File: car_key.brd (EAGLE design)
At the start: 160 x 100 mm, 2 parts, among them U2 ATMEGA328P-AU

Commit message: Major additions
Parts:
- added C10: 1pF, resistor:C0805
- added C11: 2.2nF, resistor:C0805
- added C12: 4.7pF, resistor:C0805
- added C13: 33nF, resistor:C0805
- added C14: 10nF, resistor:C0805
- added C15: 1nF, resistor:C0805
- added C16, C17: 22pF, resistor:C0805
- added C18, C7, C8: 100uF, Wurth_Elektronik_Passive_Capacitors_rev18b:3.5X1.6X2.1(BXCXA)
- added C2, C3, C4, C5, C6: 0.1uF, rcl:C0805
- added C9: 1.5pF, resistor:C0805
- added E1: ANTENNA-GROUNDEDTRACE-25.7MM, SparkFun-RF:TRACE_ANTENNA_2.4GHZ_25.7MM
- added FTDI: 61300611121, Headers:61300611121
- added I2C: 61300211121, Headers:61300211121
- added IC1: MAX3232ECD, MAX3232ECD:SOIC127P600X175-16N
- added IC2: LM1117MPX-3.3_NOPB, LM1117MPX-3.3_NOPB:SOT230P700X180-4N
- added IC3: NRF24L01P-R7, NRF24L01P-R7:QFN50P400X400X95-21N
- added IC4: LM1117MPX-5.0_NOPB, LM1117MPX-5.0_NOPB:SOT230P700X180-4N
- added L1: 8.2nH, rcl:L2012C
- added L2: 2.7nH, rcl:L2012C
- added L3: 3.9nH, rcl:L2012C
- added Q1: 16M, crystal:HC49/S
- added R1, R2, R3, R4: (no value), rcl:R0805
- added R5, R6: 1K, rcl:R0805
- added R7: 1M, rcl:R0805
- added R8: 22K, rcl:R0805
- added R9: 10K, rcl:R0805
- added RS232: (no value), Wurth_Elektronik_Electromechanic_Input-Output_Connectors_rev19b:61800929321
- added Y1: 8MHz, SparkFun-Clocks:RESONATOR-SMD-3.2X1.3
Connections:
- new net CE: IC3.1
- new net CSN: IC3.2
- new net DTR: FTDI.6
- new net FTDI_VCC: FTDI.3
- new net INT: IC3.6
- new net MISO: IC3.5
- new net MOSI: IC3.4
- new net N$10: C4.1, IC1.4
- new net N$11: C6.1, IC1.2
- new net N$12: IC1.13, RS232.3
- new net N$13: IC1.14, RS232.2
- new net N$14: IC3.13, L1.1, L3.1
- new net N$15: IC3.12, L1.2, L2.1
- new net N$16: C11.1, C12.1, IC3.11, L2.2
- new net N$17: C9.1, L3.2
- new net N$18: C10.2, C9.2, E1.ANT
- new net N$19: C13.1, IC3.19
- new net N$2: R7.2, U2.7, Y1.1
- new net N$21: C16.2, IC3.9, Q1.1, R9.1
- new net N$22: C17.2, IC3.10, Q1.2, R9.2
- new net N$23: IC3.16, R8.1
- new net N$3: R7.1, U2.8, Y1.3
- new net N$4: IC1.11, R5.1
- new net N$5: IC1.12, R6.1
- new net N$6: C5.1, IC1.6
- new net N$7: C3.2, IC1.1
- new net N$8: C4.2, IC1.5
- new net N$9: C3.1, IC1.3
- new net RAW: C8.1, IC2.3, IC4.3
- new net RX-I: FTDI.4, R2.1, R4.2, R6.2, U2.30
- new net SCK: IC3.3
- new net SCL: I2C.2, U2.28
- new net SDA: I2C.1, U2.27
- new net TX-O: FTDI.5, R1.1, R3.2, R5.2, U2.31
- new net VCC/2: C18.1, IC4.2, IC4.4
- net GND: now also C10.1, C11.2, C12.2, C13.2, C14.2, C15.2, C16.1, C17.1, C18.2, C2.2, C5.2, C7.2, C8.2, E1.GND, E1.GND2, FTDI.1, FTDI.2, IC1.15, IC2.1, IC3.14, IC3.17, IC3.20, IC3.8, IC4.1, R1.2, R2.2, R8.2, RS232.5, Y1.2
- net VCC: now also C14.1, C15.1, C2.1, C6.2, C7.1, IC1.16, IC2.2, IC2.4, IC3.15, IC3.18, IC3.7, R3.1, R4.1

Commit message: progress
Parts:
- removed FTDI: 61300611121, Headers:61300611121
- removed I2C: 61300211121, Headers:61300211121
- removed R3, R4: (no value), rcl:R0805
- removed R5, R6: 1K, rcl:R0805
- removed RS232: (no value), Wurth_Elektronik_Electromechanic_Input-Output_Connectors_rev19b:61800929321
- added C19, C20: 0.1uF, rcl:C0805
- added D1, D2: (no value), diode:SOD123
- added JP1: ICSP, pinhead:2X03
- added JP2: FTDI, pinhead:1X06
- added JP3: Digital 2, pinhead:1X06
- added JP4: Analog, pinhead:1X06
- added JP5: Digital 1, pinhead:1X08
- added JP6: Power, pinhead:1X06
- added JP7: Battery, pinhead:2X02
- added R10, R11: 10k, rcl:R0805
- added R12: 10K, rcl:R0805
- added SJ1: (no value), jumper:SJ
- added X1: 2510-, con-3m:PAK100/2500-10
- R1, R2: value (none) -> 1K
- moved R1 302.8 mm to (-81.3, -309.9)
- moved R2 302.8 mm to (-81.3, -315.0)
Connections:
- removed net RAW: C8.1, IC2.3, IC4.3
- new net BAT: C8.1, D2.A, JP7.1, JP7.3
- new net N$20: JP4.6, U2.23
- new net N$24: JP4.5, U2.24
- new net N$25: JP4.4, U2.25
- new net N$26: JP4.3, U2.26
- new net N$27: D1.C, D2.C, IC2.3, IC4.3
- new net N$28: C20.2, SJ1.1
- new net N$29: JP5.4, U2.1
- new net N$30: JP5.5, U2.2
- new net N$31: JP5.6, U2.9
- new net N$32: JP5.7, U2.10
- new net RESET: C20.1, JP1.5, JP6.5, R12.1, U2.29
- new net S_LOCK: JP3.6, U2.12
- new net S_UNLOCK: JP5.8, U2.11
- net CE: now also JP3.5, U2.13
- net CSN: now also JP3.4, U2.14
- net DTR: now also JP2.1, SJ1.2; no longer FTDI.6
- net FTDI_VCC: now also D1.A, JP2.4; no longer FTDI.3
- net GND: now also C19.2, JP1.6, JP2.5, JP2.6, JP6.1, JP6.2, JP7.2, JP7.4, X1.5; no longer FTDI.1, FTDI.2, R1.2, R2.2, RS232.5
- net INT: now also JP5.3, U2.32
- net MISO: now also JP1.1, JP3.2, U2.16
- net MOSI: now also JP1.4, JP3.3, U2.15
- net N$12: now also X1.3; no longer RS232.3
- net N$13: now also X1.2; no longer RS232.2
- net N$4: now also JP5.1, R1.1; no longer IC1.11, R5.1
- net N$5: now also JP5.2, R2.1; no longer IC1.12, R6.1
- net RX-I: now also IC1.12, JP2.3, R1.2; no longer FTDI.4, R2.1, R4.2, R6.2
- net SCK: now also JP1.3, JP3.1, U2.17
- net SCL: now also JP4.1, R10.1; no longer I2C.2
- net SDA: now also JP4.2, R11.1; no longer I2C.1
- net TX-O: now also IC1.11, JP2.2, R2.2; no longer FTDI.5, R1.1, R3.2, R5.2
- net VCC: now also C19.1, JP1.2, JP6.4, JP6.6, R10.2, R11.2, R12.2; no longer R3.1, R4.1
- net VCC/2: now also JP6.3

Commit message: changes
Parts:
- added Q2: BSS816NWH6327XTSA1, BSS816NWH6327XTSA1:SOT65P210X100-3N
- added R3, R4: 10K, rcl:R0805
- added R5: 2K, rcl:R0805
- added SW1, SW2: B3U-1000P, Switch:B3U-1000P
- added U$1, U$2, U$3, U$4: (no value), holes:3,2
- added U$5: (no value), SparkFun-Aesthetics:OSHW-LOGO-L
- moved X1 341.9 mm to (76.2, 6.35)
- moved D2 290.4 mm to (-120.7, -69.8)
- moved D1 290.4 mm to (-120.7, -64.8)
- moved JP7 248.0 mm to (-127.0, -99.1)
- moved C20 233.8 mm to (-92.7, -52.1)
- moved JP1 233.8 mm to (-96.5, -78.7)
- moved JP3 233.8 mm to (-91.4, -95.2)
- moved JP5 233.8 mm to (-88.9, -108.0)
- moved JP6 233.8 mm to (-91.4, -115.6)
- moved R1 233.8 mm to (-88.9, -76.2)
- moved R10 233.8 mm to (-92.7, -35.6)
- moved R11 233.8 mm to (-92.7, -40.6)
- moved SJ1 233.8 mm to (-92.7, -58.4)
- moved C19 233.8 mm to (-92.7, -19.1)
- moved JP2 233.8 mm to (-91.4, -88.9)
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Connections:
- removed net N$20: JP4.6, U2.23
- removed net N$32: JP5.7, U2.10
- new net N$33: D2.A, Q2.2, SW1.2
- new net S_POWER: JP5.7, Q2.1, R3.2, U2.10
- new net V_SENSE: JP4.6, R4.1, R5.2, U2.23
- net BAT: now also Q2.3, R4.2, SW1.1; no longer D2.A
- net GND: now also R3.1, R5.1, SW2.1
- net RESET: now also SW2.2
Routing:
- net VCC: track 0.00 -> 20.5 mm, vias 0 -> 2
- net N$12: track 0.00 -> 15.5 mm
- net N$9: track 0.00 -> 13.7 mm
- net N$13: track 0.00 -> 10.9 mm
- net N$10: track 0.00 -> 6.83 mm
- net N$11: track 0.00 -> 4.75 mm
- net N$8: track 0.00 -> 4.22 mm
- net N$7: track 0.00 -> 4.22 mm
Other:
- board size 160 x 100 mm -> 100 x 100 mm
- board text added: "github.com/olback/car-key"

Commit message: changes
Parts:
- removed IC4: LM1117MPX-5.0_NOPB, LM1117MPX-5.0_NOPB:SOT230P700X180-4N
- removed JP2: FTDI, pinhead:1X06
- removed JP3: Digital 2, pinhead:1X06
- removed JP4: Analog, pinhead:1X06
- removed JP5: Digital 1, pinhead:1X08
- removed JP6: Power, pinhead:1X06
- removed JP7: Battery, pinhead:2X02
- added FTDI: TSW-106-08-G-S, con-samtec:TSW-106-XX-G-S
- added I2C: TSW-102-08-G-S, con-samtec:TSW-102-XX-G-S
- added JP8: nRF24L01+ Module, pinhead:2X04
- X1: value 2510- -> RS232
- moved C17 257.3 mm to (152.4, 30.5), turned to 180 degrees
- moved R9 246.1 mm to (143.5, 35.1)
- moved C16 245.2 mm to (134.6, 30.5)
- moved C15 241.8 mm to (139.7, 47.0), turned to 90 degrees
- moved C14 241.3 mm to (142.2, 47.0), turned to 90 degrees
- moved C13 240.4 mm to (144.8, 47.0), turned to 90 degrees
- moved R8 239.7 mm to (147.3, 47.0), turned to 90 degrees
- moved C12 239.6 mm to (154.9, 36.8)
- moved C10 238.7 mm to (154.9, 44.5)
- moved C11 238.7 mm to (154.9, 39.4)
- moved Q1 237.2 mm to (143.5, 30.5)
- moved C9 235.9 mm to (154.9, 41.9)
- moved L3 229.8 mm to (151.1, 43.2), turned to 270 degrees
- moved R1 225.8 mm to (118.1, 14.0), turned to 270 degrees
- moved R2 225.6 mm to (115.6, 14.0), turned to 270 degrees
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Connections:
- removed net N$24: JP4.5, U2.24
- removed net N$25: JP4.4, U2.25
- removed net N$26: JP4.3, U2.26
- removed net N$29: JP5.4, U2.1
- removed net N$30: JP5.5, U2.2
- removed net N$31: JP5.6, U2.9
- net BAT: no longer JP7.1, JP7.3
- net CE: now also JP8.3; no longer JP3.5
- net CSN: now also JP8.4; no longer JP3.4
- net DTR: now also FTDI.1; no longer JP2.1
- net FTDI_VCC: now also FTDI.4; no longer JP2.4
- net GND: now also FTDI.5, FTDI.6, JP8.1; no longer IC4.1, JP2.5, JP2.6, JP6.1, JP6.2, JP7.2, JP7.4
- net INT: now also JP8.8; no longer JP5.3
- net MISO: now also JP8.7; no longer JP3.2
- net MOSI: now also JP8.6; no longer JP3.3
- net N$27: no longer IC4.3
- net N$4: now also U2.31; no longer JP5.1
- net N$5: now also U2.30; no longer JP5.2
- net RESET: no longer JP6.5
- net RX-I: now also FTDI.3, R2.2; no longer JP2.3, R1.2, U2.30
- net SCK: now also JP8.5; no longer JP3.1
- net SCL: now also I2C.1; no longer JP4.1
- net SDA: now also I2C.2; no longer JP4.2
- net S_LOCK: no longer JP3.6
- net S_POWER: no longer JP5.7
- net S_UNLOCK: no longer JP5.8
- net TX-O: now also FTDI.2, R1.2; no longer JP2.2, R2.2, U2.31
- net VCC: now also JP8.2; no longer JP6.4, JP6.6
- net VCC/2: no longer IC4.2, IC4.4, JP6.3
- net V_SENSE: no longer JP4.6
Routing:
- net MISO: track 0.00 -> 104.6 mm, vias 0 -> 2
- net SCK: track 0.00 -> 101.7 mm, vias 0 -> 2
- net MOSI: track 0.00 -> 97.1 mm, vias 0 -> 2
- net RX-I: track 0.00 -> 64.7 mm, vias 0 -> 1
- net TX-O: track 0.00 -> 60.7 mm, vias 0 -> 1
- net CE: track 0.00 -> 59.7 mm, vias 0 -> 2
- net CSN: track 0.00 -> 58.7 mm, vias 0 -> 2
- net RESET: track 0.00 -> 46.8 mm
- net VCC: track 20.5 -> 60.4 mm, vias 2 -> 4
- net INT: track 0.00 -> 37.5 mm
- net N$21: track 0.00 -> 15.2 mm
- net N$22: track 0.00 -> 14.4 mm
- net N$16: track 0.00 -> 12.2 mm
- net N$14: track 0.00 -> 8.40 mm
- net N$18: track 0.00 -> 7.41 mm
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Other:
- board size 100 x 100 mm -> 168 x 70 mm
- board text added: "Central Comfort Module Connector"

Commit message: changes
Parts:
- removed C8: 100uF, Wurth_Elektronik_Passive_Capacitors_rev18b:3.5X1.6X2.1(BXCXA)
- removed IC2: LM1117MPX-3.3_NOPB, LM1117MPX-3.3_NOPB:SOT230P700X180-4N
- removed Q2: BSS816NWH6327XTSA1, BSS816NWH6327XTSA1:SOT65P210X100-3N
- added C21: 10u, Wurth_Elektronik_Passive_Capacitors_rev18b:2.6X1.6X1(BXCXA)
- added IC4: TPS562231DRLR, TPS562231DRLR:SOTFL50P160X60-6N
- added L4: DFE322520FD-3R3M=P2, DFE322520FD-3R3M=P2:INDC3225X200N
- added Q3: FDN360P, transistor-power:SUPER-SOT3
- added R13: 2.2k, rcl:R0805
- added R14: 100, rcl:R0805
- added R15: 10k, rcl:R0805
- added R6: 43k, rcl:R0805
- C18: value 100uF -> 0.1u; device Wurth_Elektronik_Passive_Capacitors_rev18b:3.5X1.6X2.1(BXCXA) -> rcl:C0805
- C7: value 100uF -> 47u; device Wurth_Elektronik_Passive_Capacitors_rev18b:3.5X1.6X2.1(BXCXA) -> Wurth_Elektronik_Passive_Capacitors_rev18b:2.6X1.6X1(BXCXA)
- moved SW2 273.6 mm to (106.7, 26.7), turned to 90 degrees
- moved SW1 215.0 mm to (22.9, 46.2), turned to 270 degrees
- moved SJ1 211.3 mm to (102.9, 21.6), turned to 270 degrees
- moved C20 210.8 mm to (102.9, 26.7), turned to 270 degrees
- moved Y1 209.5 mm to (111.8, 29.2)
- moved R5 208.5 mm to (25.4, 52.1), turned to 270 degrees
- moved R7 207.2 mm to (111.8, 31.8), turned to 180 degrees
- moved R12 206.2 mm to (100.3, 26.7), turned to 270 degrees
- moved C19 205.8 mm to (106.7, 31.8), turned to 180 degrees
- moved R4 202.3 mm to (22.9, 52.1), turned to 90 degrees
- moved R3 202.0 mm to (27.9, 52.1), turned to 270 degrees
- moved D2 190.6 mm to (30.5, 46.2), turned to 270 degrees
- moved D1 189.6 mm to (33.0, 46.2), turned to 270 degrees
- moved C18 185.4 mm to (43.2, 52.1), turned to 90 degrees
- moved C7 172.2 mm to (43.2, 46.2), turned to 90 degrees
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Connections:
- removed net VCC/2: C18.1
- new net N$24: C18.1, IC4.2, L4.1
- new net N$25: C18.2, IC4.4
- new net N$26: R13.2, R14.2
- new net N$30: R13.1, R6.1
- new net N$31: IC4.6, R14.1, R15.2
- net BAT: now also Q3.2; no longer C8.1, Q2.3
- net GND: now also C21.2, IC4.3, R15.1; no longer C18.2, C8.2, IC2.1
- net N$27: now also C21.1, IC4.1, IC4.5; no longer IC2.3
- net N$33: now also Q3.3; no longer Q2.2
- net S_POWER: now also Q3.1; no longer Q2.1
- net VCC: now also L4.2, R6.2; no longer IC2.2, IC2.4
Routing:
- net VCC: track 60.4 -> 256.2 mm, vias 4 -> 8
- net SCL: track 0.00 -> 65.9 mm, vias 0 -> 1
- net SDA: track 0.00 -> 64.5 mm, vias 0 -> 1
- net INT: track 37.5 -> 82.8 mm, vias 0 -> 1
- net DTR: track 0.00 -> 30.8 mm, vias 0 -> 1
- net S_POWER: track 0.00 -> 29.3 mm
- net N$4: track 0.00 -> 29.2 mm, vias 0 -> 2
- net N$5: track 0.00 -> 28.5 mm, vias 0 -> 2
- net N$27: track 0.00 -> 14.2 mm
- net N$33: track 0.00 -> 8.73 mm
- net N$24: track 0.00 -> 7.49 mm
- net N$3: track 0.00 -> 6.42 mm
- net N$2: track 0.00 -> 6.30 mm
- net SCK: track 101.7 -> 107.5 mm
- net RESET: track 46.8 -> 52.1 mm, vias 0 -> 1
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- added copper zone on layer 1, net GND

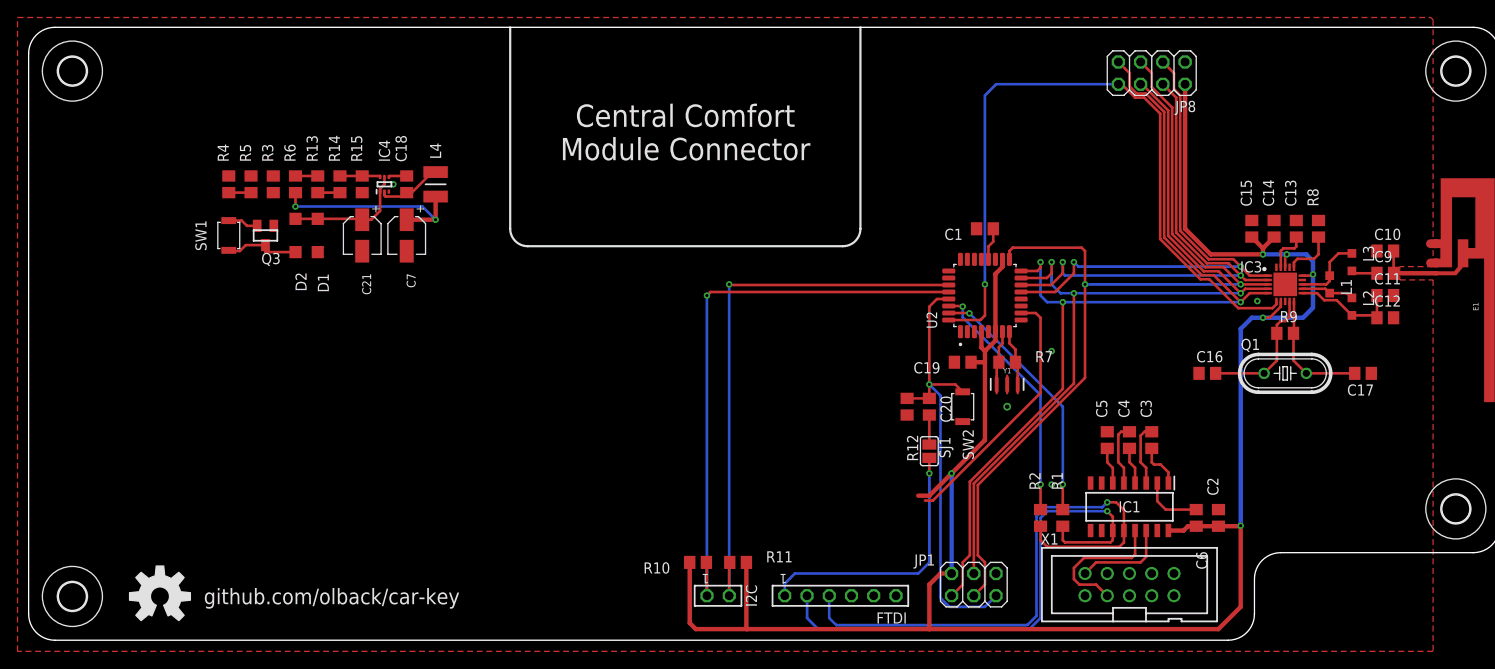
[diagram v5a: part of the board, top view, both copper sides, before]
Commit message: move psu, labels
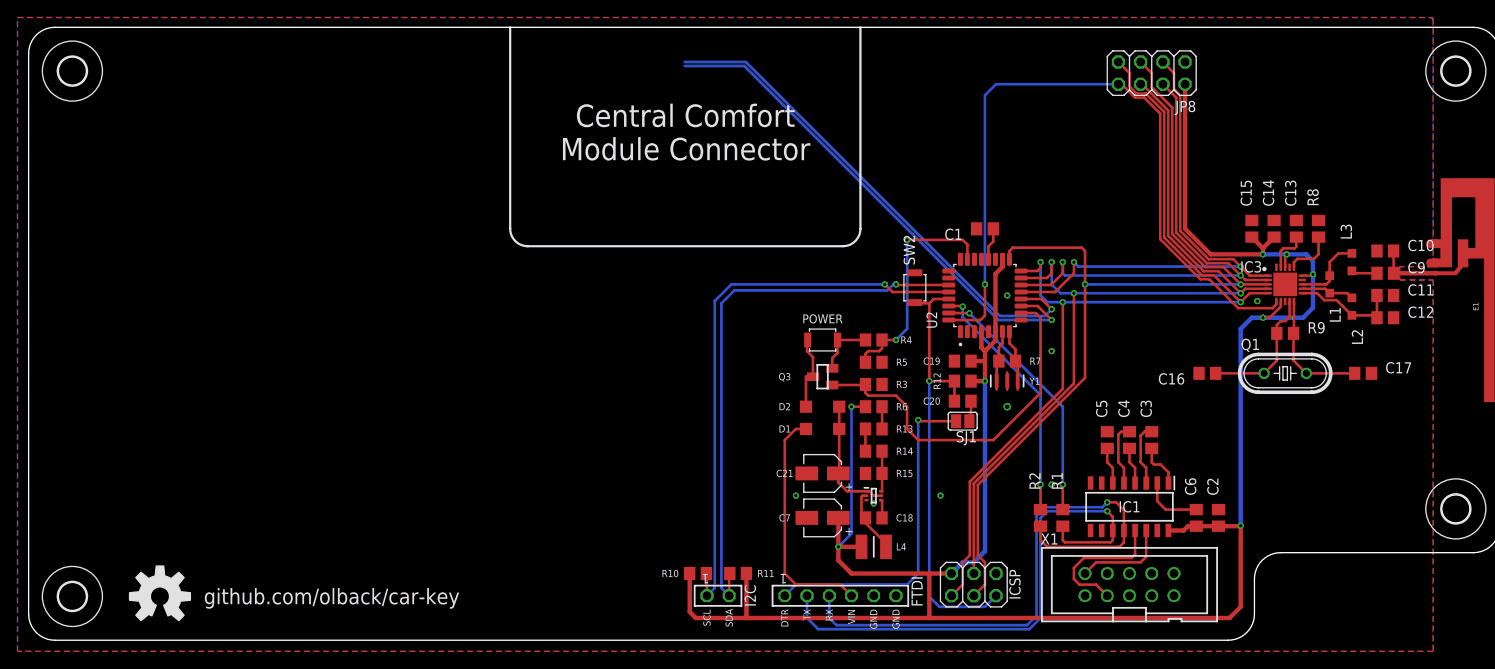
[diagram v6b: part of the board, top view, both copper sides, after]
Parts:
- removed SW1: B3U-1000P, Switch:B3U-1000P
- added POWER: B3U-1000P, Switch:B3U-1000P
- moved R4 75.8 mm to (96.5, 34.3), turned to 180 degrees
- moved R5 74.0 mm to (96.5, 31.8), turned to 180 degrees
- moved R3 72.3 mm to (96.5, 29.2), turned to 180 degrees
- moved R6 70.8 mm to (96.5, 26.7), turned to 180 degrees
- moved R13 69.4 mm to (96.5, 24.1), turned to 180 degrees
- moved R14 68.2 mm to (96.5, 21.6), turned to 180 degrees
- moved R15 67.1 mm to (96.5, 19.1), turned to 0 degrees
- moved IC4 66.2 mm to (96.5, 16.5), turned to 0 degrees
- moved Q3 65.6 mm to (90.7, 30.1), turned to 90 degrees
- moved C18 65.5 mm to (96.5, 14.0), turned to 0 degrees
- moved L4 64.9 mm to (96.5, 10.7), turned to 180 degrees
- moved D2 63.3 mm to (90.7, 26.7), turned to 180 degrees
- moved D1 61.7 mm to (90.7, 24.1), turned to 180 degrees
- moved C21 59.2 mm to (90.7, 19.1), turned to 0 degrees
- moved C7 57.4 mm to (90.7, 14.0), turned to 0 degrees
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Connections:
- net BAT: now also POWER.1; no longer SW1.1
- net N$33: now also POWER.2; no longer SW1.2
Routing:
- net S_LOCK: track 0.00 -> 58.2 mm, vias 0 -> 1
- net S_UNLOCK: track 0.00 -> 58.1 mm, vias 0 -> 1
- net FTDI_VCC: track 0.00 -> 26.9 mm
- net V_SENSE: track 2.54 -> 26.4 mm, vias 0 -> 2
- net S_POWER: track 29.3 -> 41.8 mm
- net DTR: track 30.8 -> 38.2 mm
- net VCC: track 256.2 -> 260.1 mm
- net BAT: track 3.49 -> 6.68 mm
- net SCL: track 65.9 -> 64.5 mm
- net SDA: track 64.5 -> 63.2 mm
- net N$28: track 3.37 -> 2.36 mm
- net RESET: track 52.1 -> 51.4 mm
- net GND: vias 5 -> 8
- added copper zone on layer 16, net GND
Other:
- board text added: "DTR"
- board text added: "GND"
- board text added: "RX"
- board text added: "SCL"
- board text added: "SDA"
- board text added: "TX"
- board text added: "VIN"

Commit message: aa
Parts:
- JP8: value nRF24L01+ Module -> nRF24L01+
- renumbered SW2 to RESET
